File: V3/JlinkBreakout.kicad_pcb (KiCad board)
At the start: 2 copper layers, 38.5 x 27 mm, 11 parts, among them J1 JLINK, J2 TC, J3 SWD, U1 SGM2019, U2 switch_0204

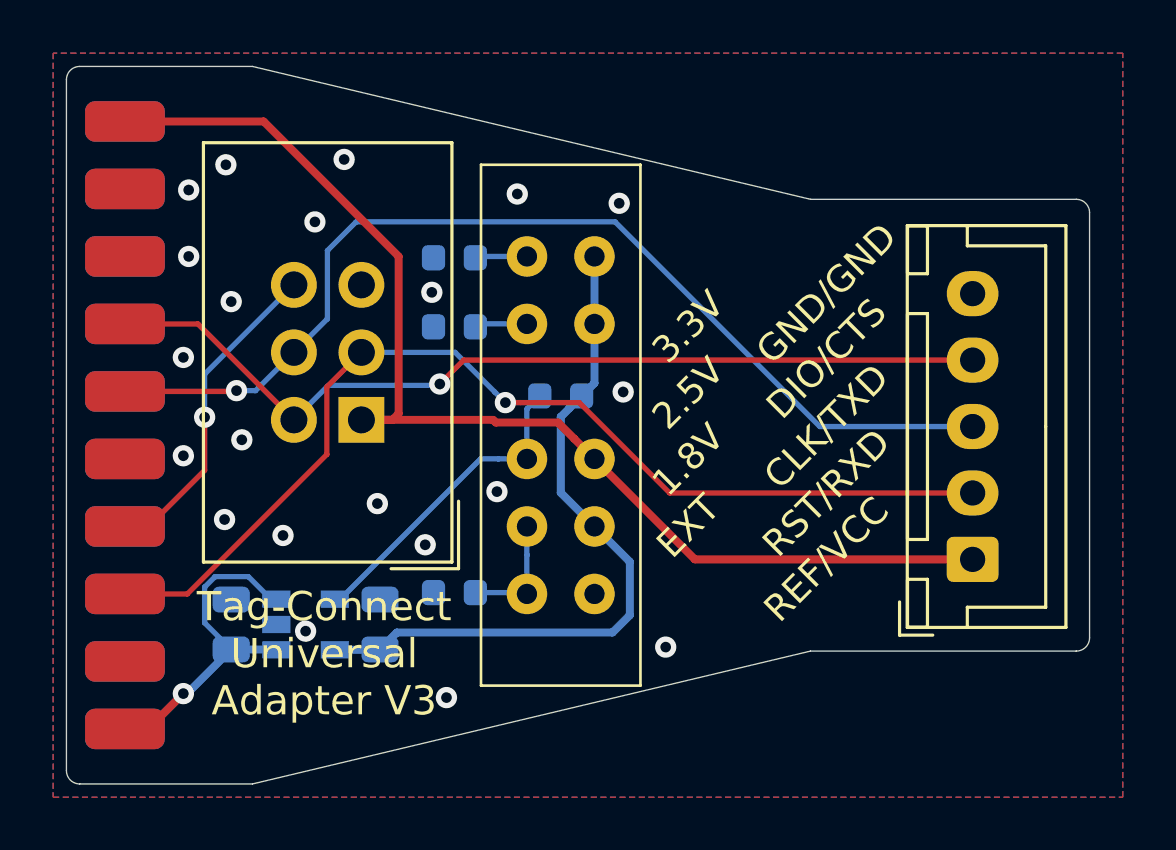
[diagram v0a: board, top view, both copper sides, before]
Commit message: fixed footprint
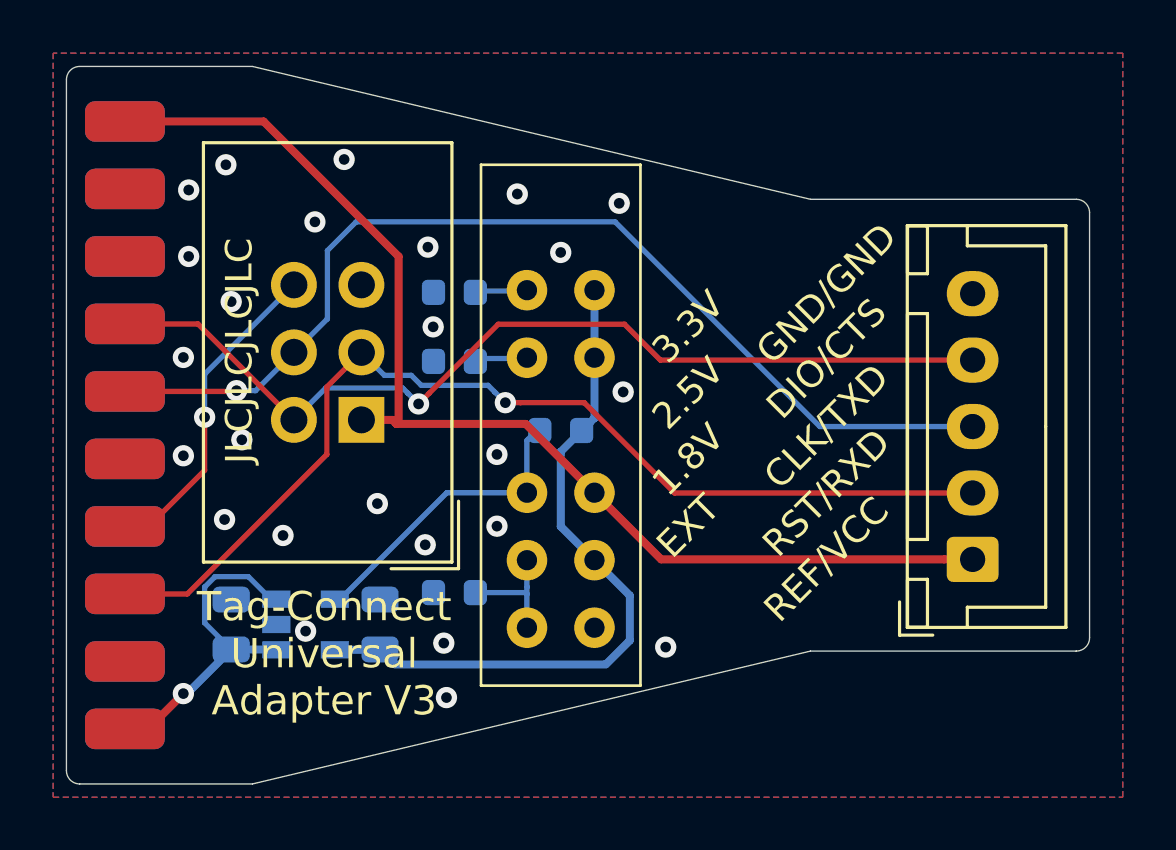
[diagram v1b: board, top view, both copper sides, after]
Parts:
- moved R1 1.30 mm to (76.6, 46.7)
- moved R3 1.30 mm to (72.6, 44.1)
- moved R4 1.30 mm to (72.6, 41.5)
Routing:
- net DIO: track 34.3 -> 35.9 mm
- net REF: track 45.0 -> 43.9 mm
- net GND: vias 21 -> 25
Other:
- board text added: "JLCJLCJLCJLC"
